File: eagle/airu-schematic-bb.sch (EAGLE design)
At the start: 26 parts, among them IC1 MCP3008, IC2 TPS77001, U1 BMP180, U2 DHT22, U3 GPS

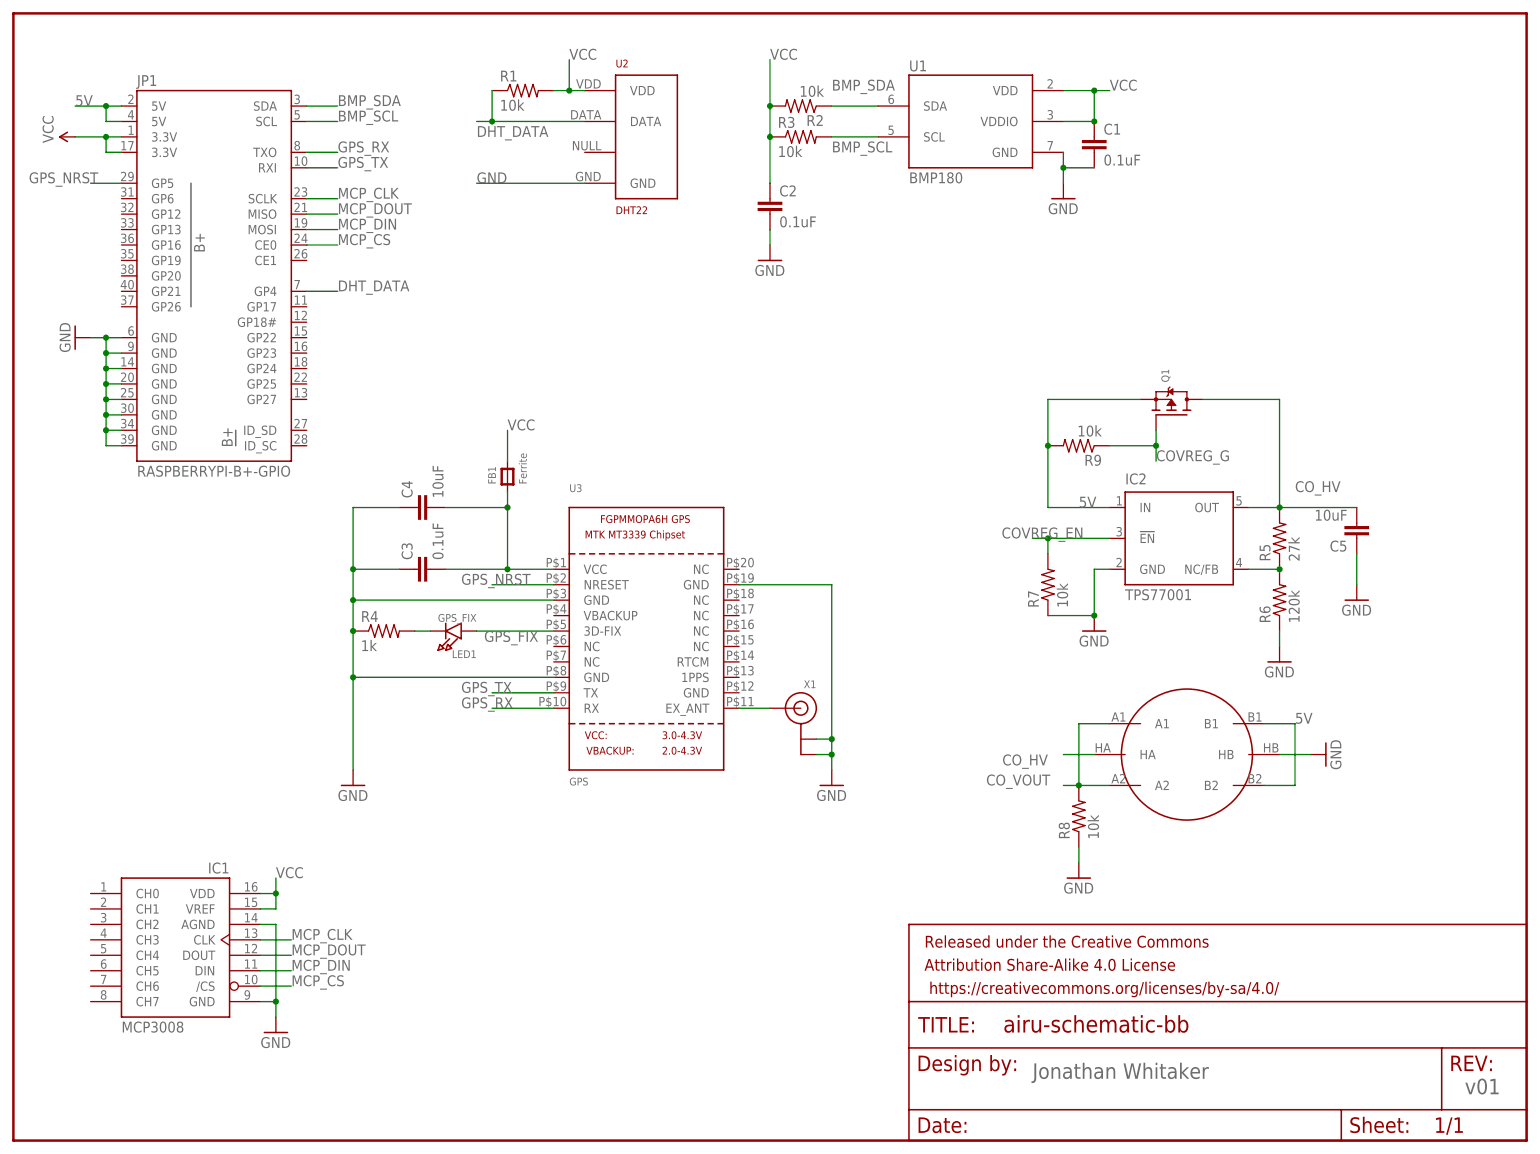
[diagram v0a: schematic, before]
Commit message: Added schematic copy for BeagleBone
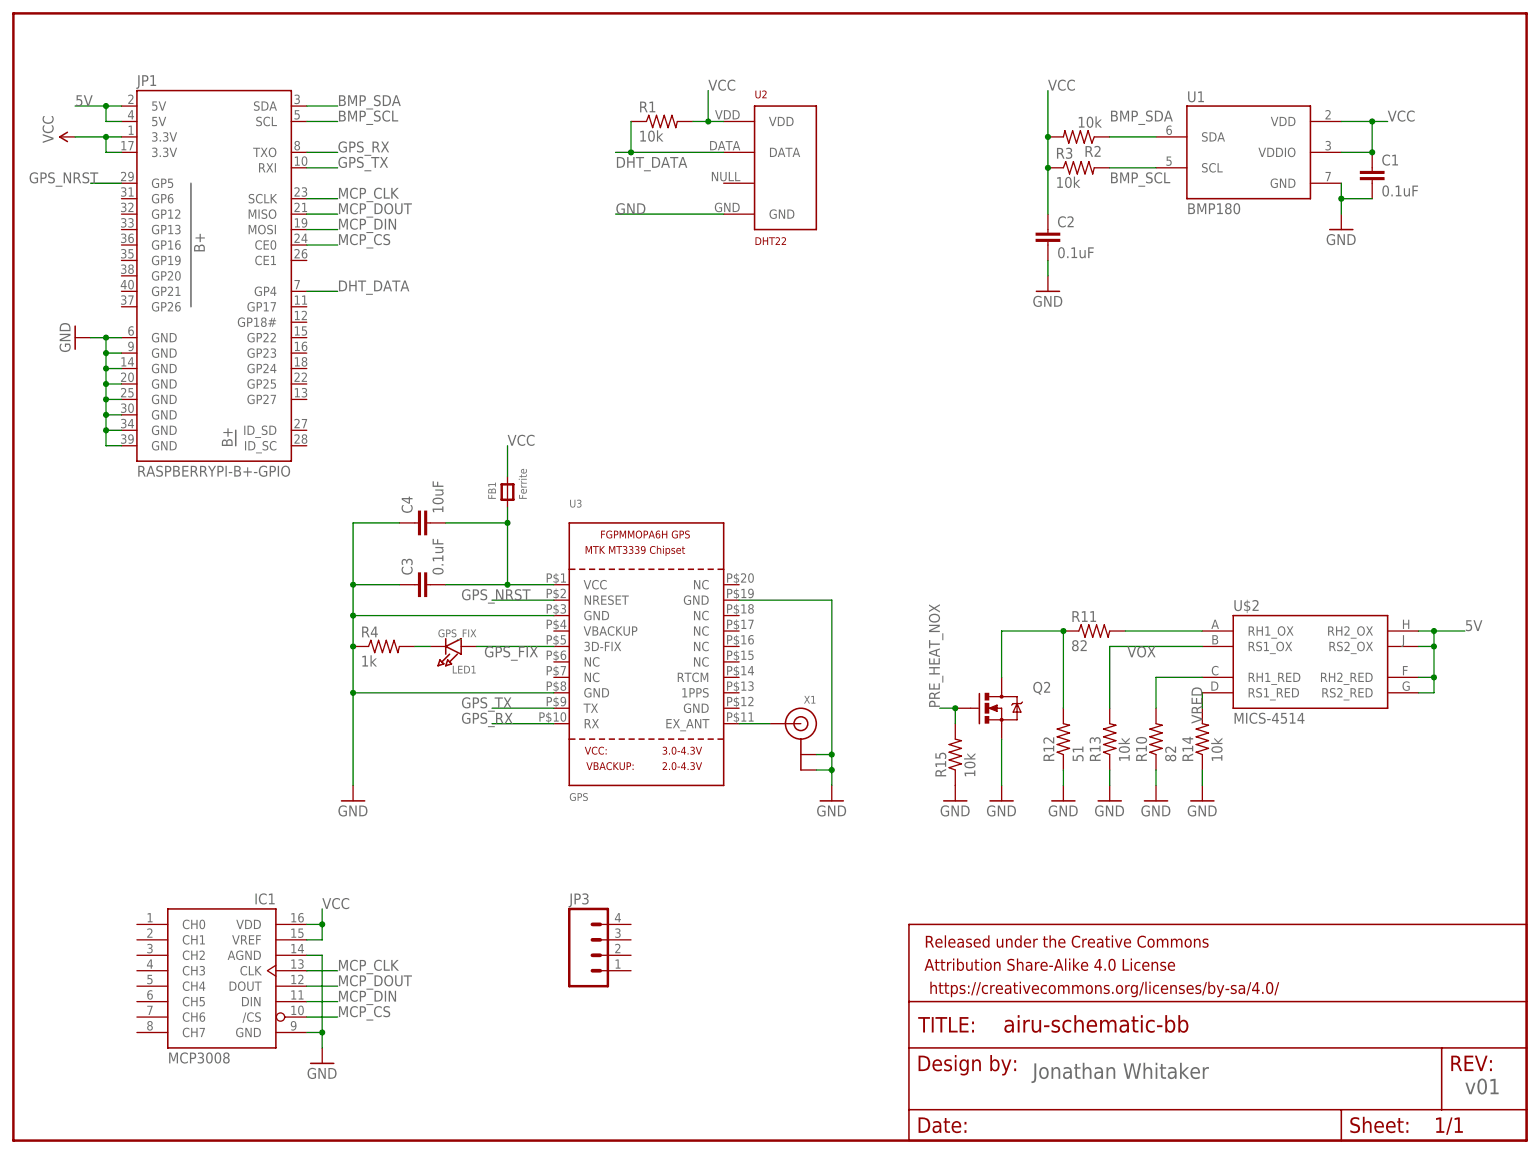
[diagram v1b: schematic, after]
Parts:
- removed C5: 10uF, SparkFun-Passives:CAP1206
- removed IC2: TPS77001, texas:TPS77001
- removed Q1: (no value), microbuilder:MOSFET-P
- removed R5: 27k, SparkFun-Passives:RESISTOR1206
- removed R6: 120k, SparkFun-Passives:RESISTOR1206
- removed R7, R8, R9: 10k, SparkFun-Passives:RESISTOR1206
- removed U$1: METHANE_SENSOR, SparkFun-Sensors:METHANE_SENSOR
- added JP3: (no value), SparkFun-Connectors:M04JST-PTH
- added Q2: MOSFET-NCHANNELAO3404A, SparkFun-DiscreteSemi:MOSFET-NCHANNELAO3404A
- added R10, R11: 82, SparkFun-Passives:RESISTOR1206
- added R12: 51, SparkFun-Passives:RESISTOR1206
- added R13, R14, R15: 10k, SparkFun-Passives:RESISTOR1206
- added U$2: MICS-4514, SparkFun-Sensors:MICS-4514
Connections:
- removed net COVREG_EN: IC2.!EN, R7.2
- removed net COVREG_G: Q1.G, R9.1
- removed net CO_HV: C5.2, IC2.OUT, Q1.D, R5.2, U$1.HA
- removed net CO_VOUT: R8.2, U$1.A1, U$1.A2
- removed net N$5: IC2.NC/FB, R5.1, R6.2
- new net N$4: R10.2, U$2.RH1_RED
- new net N$7: Q2.D, R11.1, R12.2
- new net N$9: R11.2, U$2.RH1_OX
- new net PRE_HEAT_NOX: Q2.G, R15.2
- new net VOX: R13.2, U$2.RS1_OX
- new net VRED: R14.2, U$2.RS1_RED
- net 5V: now also U$2.RH2_OX, U$2.RH2_RED, U$2.RS2_OX, U$2.RS2_RED; no longer IC2.IN, Q1.S, R9.2, U$1.B1, U$1.B2
- net GND: now also Q2.S, R10.1, R12.1, R13.1, R14.1, R15.1; no longer C5.1, IC2.GND, R6.1, R7.1, R8.1, U$1.HB
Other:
- note removed: "MQ-7 CO"
- moved on the sheet: C1, C2, C3, C4, FB1, IC1, LED1, R1, R2, R3, R4, U1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

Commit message: Added schematic for BeagleBone Black
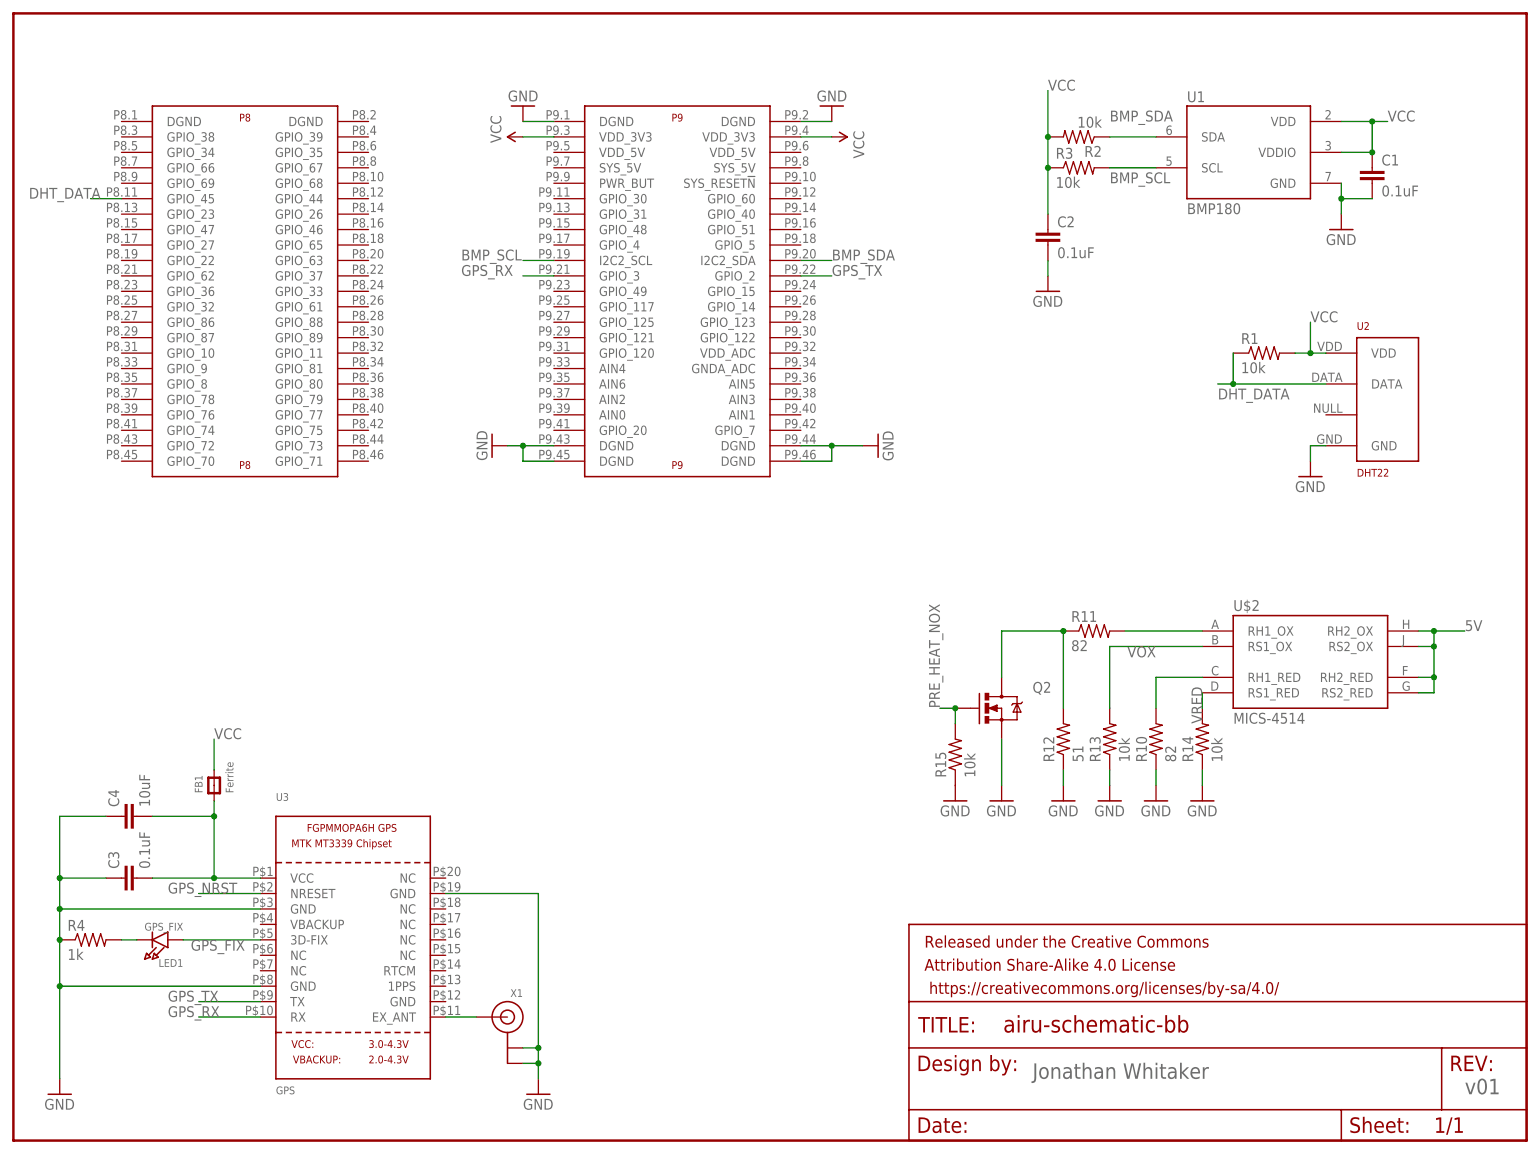
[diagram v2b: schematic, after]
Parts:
- removed IC1: MCP3008, adafruit:MCP3008
- removed JP1: RASPBERRYPI-B+-GPIO, SparkFun-Boards:RASPBERRYPI-B+-GPIO
- removed JP3: (no value), SparkFun-Connectors:M04JST-PTH
- added U$1: BEAGLE_BONE_BLACK_CAPE, SparkFun-Boards:BEAGLE_BONE_BLACK_CAPE
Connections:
- removed net MCP_CLK: IC1.CLK, JP1.SCLK
- removed net MCP_CS: IC1./CS, JP1.CE0
- removed net MCP_DIN: IC1.DIN, JP1.MOSI
- removed net MCP_DOUT: IC1.DOUT, JP1.MISO
- net 5V: no longer JP1.5V@2, JP1.5V@4
- net BMP_SCL: now also U$1P9.I2C2_SCL; no longer JP1.SCL
- net BMP_SDA: now also U$1P9.I2C2_SDA; no longer JP1.SDA
- net DHT_DATA: now also U$1P8.GPIO_45; no longer JP1.GP4
- net GND: now also U$1P9.DGND@1, U$1P9.DGND@2, U$1P9.DGND@3, U$1P9.DGND@4, U$1P9.DGND@5, U$1P9.DGND@6; no longer IC1.AGND, IC1.GND, JP1.GND@14, JP1.GND@20, JP1.GND@25, JP1.GND@30, JP1.GND@34, JP1.GND@39, JP1.GND@6, JP1.GND@9
- net GPS_NRST: no longer JP1.GP5
- net GPS_RX: now also U$1P9.GPIO_3; no longer JP1.TXO
- net GPS_TX: now also U$1P9.GPIO_2; no longer JP1.RXI
- net VCC: now also U$1P9.VDD_3V3@1, U$1P9.VDD_3V3@2; no longer IC1.VDD, IC1.VREF, JP1.3.3V@1, JP1.3.3V@17
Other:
- moved on the sheet: C3, C4, FB1, LED1, R1, R4, U2, U3, X1

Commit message: Updated BOM and added slight improvements to the PCB layout.
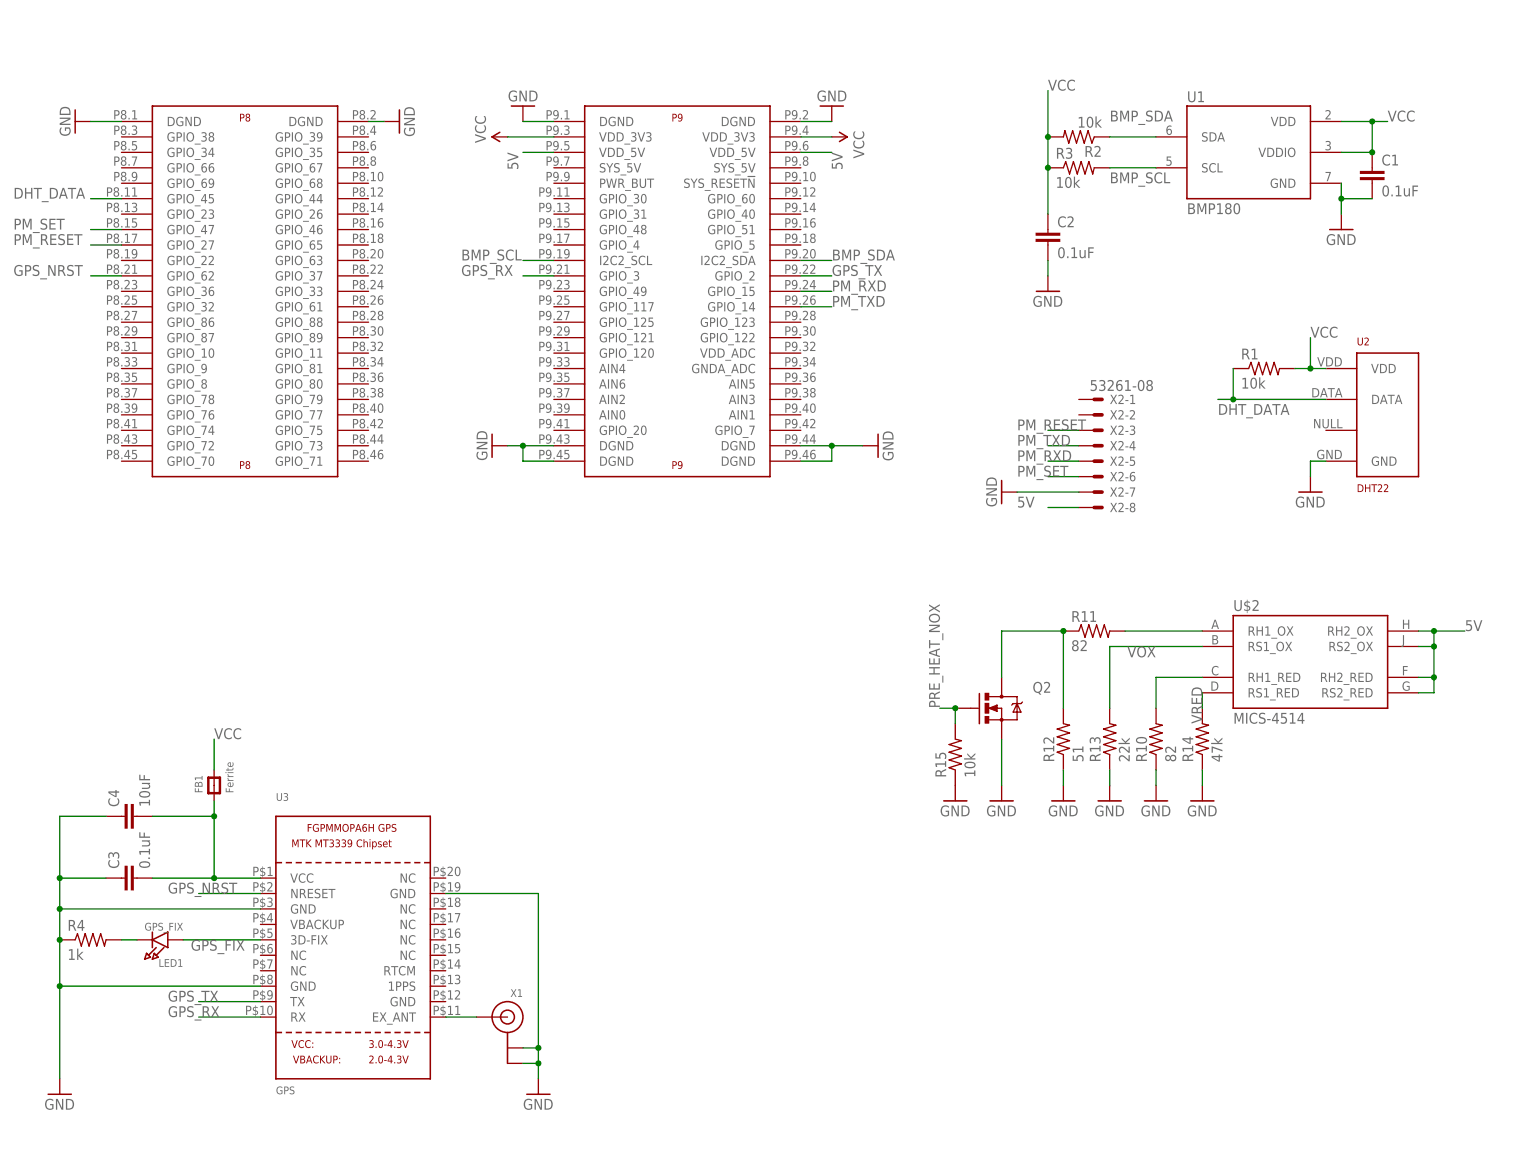
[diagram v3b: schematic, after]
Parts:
- removed FRAME1: (no value), SparkFun-Aesthetics:FRAME-LETTER
- added X2: 53261-08, con-molex:53261-08
- R13: value 10k -> 22k
- R14: value 10k -> 47k
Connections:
- new net PM_RESET: U$1P8.GPIO_27, X2-3.S
- new net PM_RXD: U$1P9.GPIO_15, X2-5.S
- new net PM_SET: U$1P8.GPIO_47, X2-6.S
- new net PM_TXD: U$1P9.GPIO_14, X2-4.S
- net 5V: now also U$1P9.VDD_5V@1, U$1P9.VDD_5V@2, X2-8.S
- net GND: now also U$1P8.DGND@1, U$1P8.DGND@2, X2-7.S
- net GPS_NRST: now also U$1P8.GPIO_62
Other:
- moved on the sheet: R1, U2
